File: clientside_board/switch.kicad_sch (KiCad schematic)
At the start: 23 parts, among them J5 Screw_Terminal_01x11, J6 Screw_Terminal_01x12, J7 Fire Button Connector, J8 Keylock Switch Connector, Q1 TSM2306CX

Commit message: Cleanup Power and Ethernet Sheet
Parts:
- renumbered J8 to J10, J5 to J7, J6 to J8, J7 to J9, R24 to R13, R8 to R14, R25 to R15, R9 to R16, R26 to R17, R10 to R18, R27 to R19, R11 to R20, R13 to R21, R16 to R22, R12 to R23, R17 to R24, R5 to R25, R14 to R26, R18 to R27, R6 to R28, R7 to R29, R15 to R30

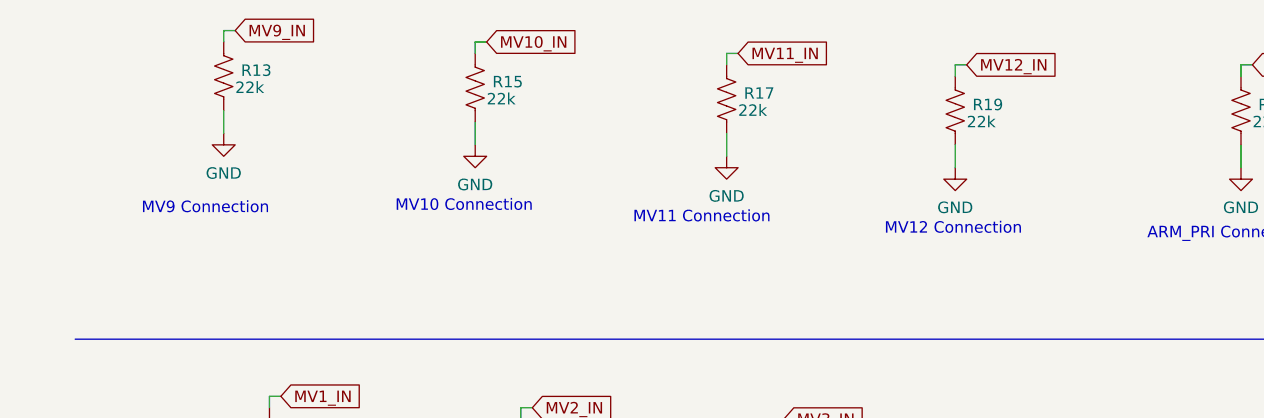
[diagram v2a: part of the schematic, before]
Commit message: Fix decoupling cap
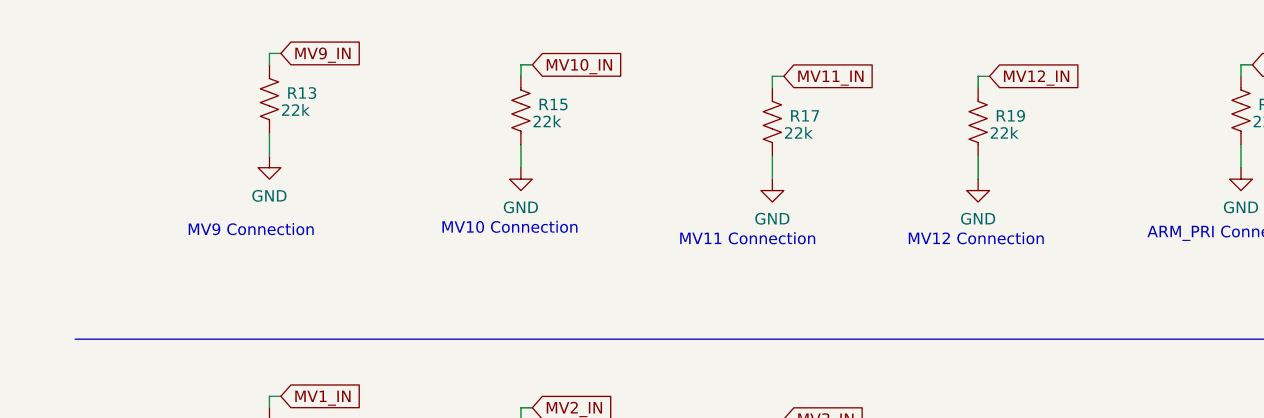
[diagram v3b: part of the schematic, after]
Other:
- moved on the sheet: R13, R15, R17, R19

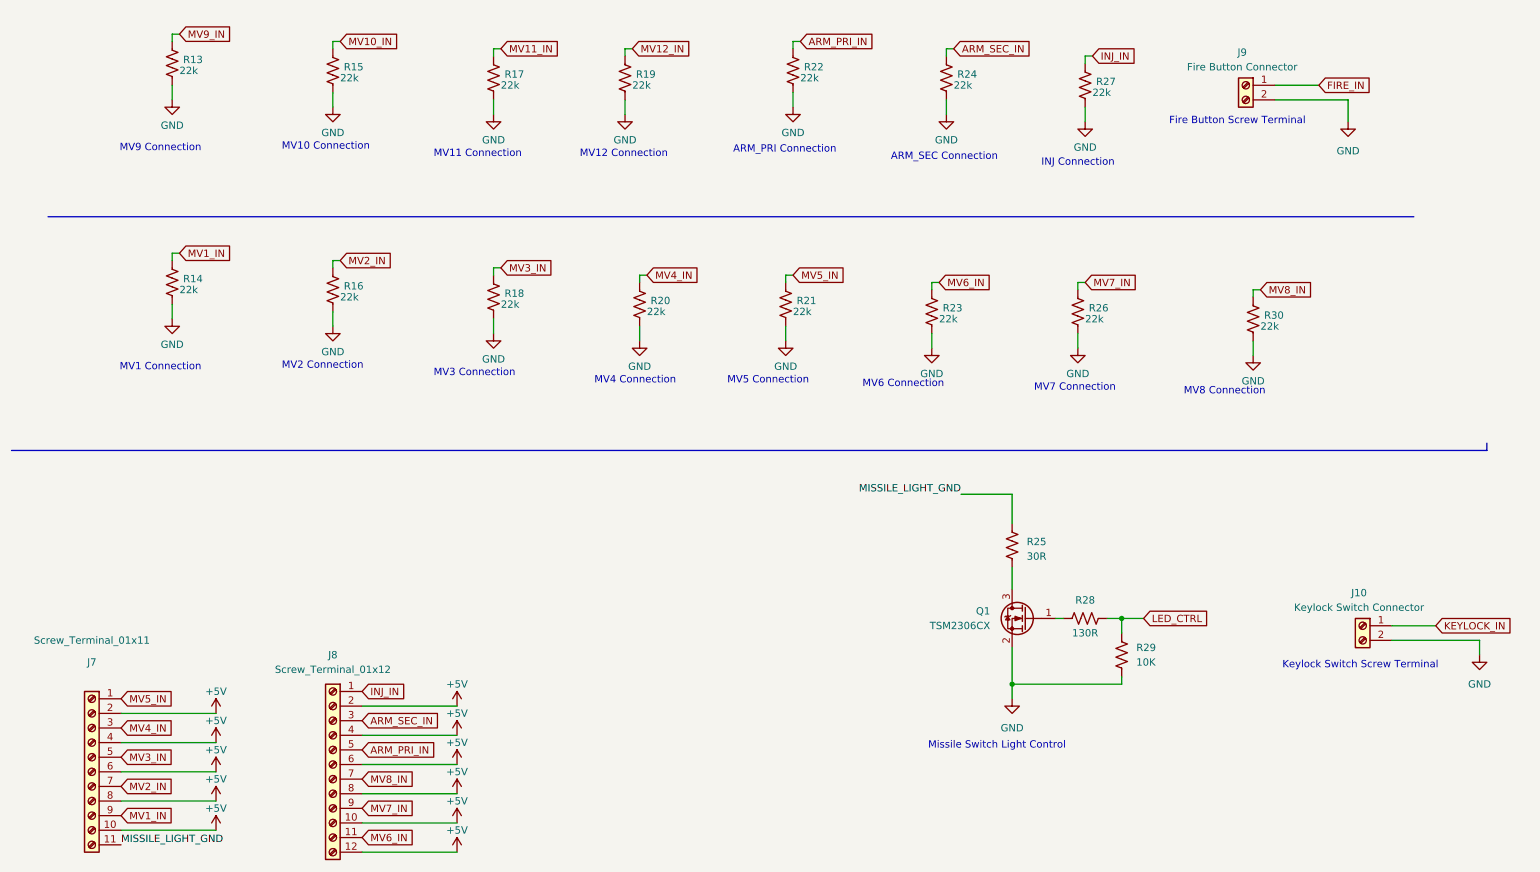
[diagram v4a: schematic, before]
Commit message: Clean-up missile switch connection sheet
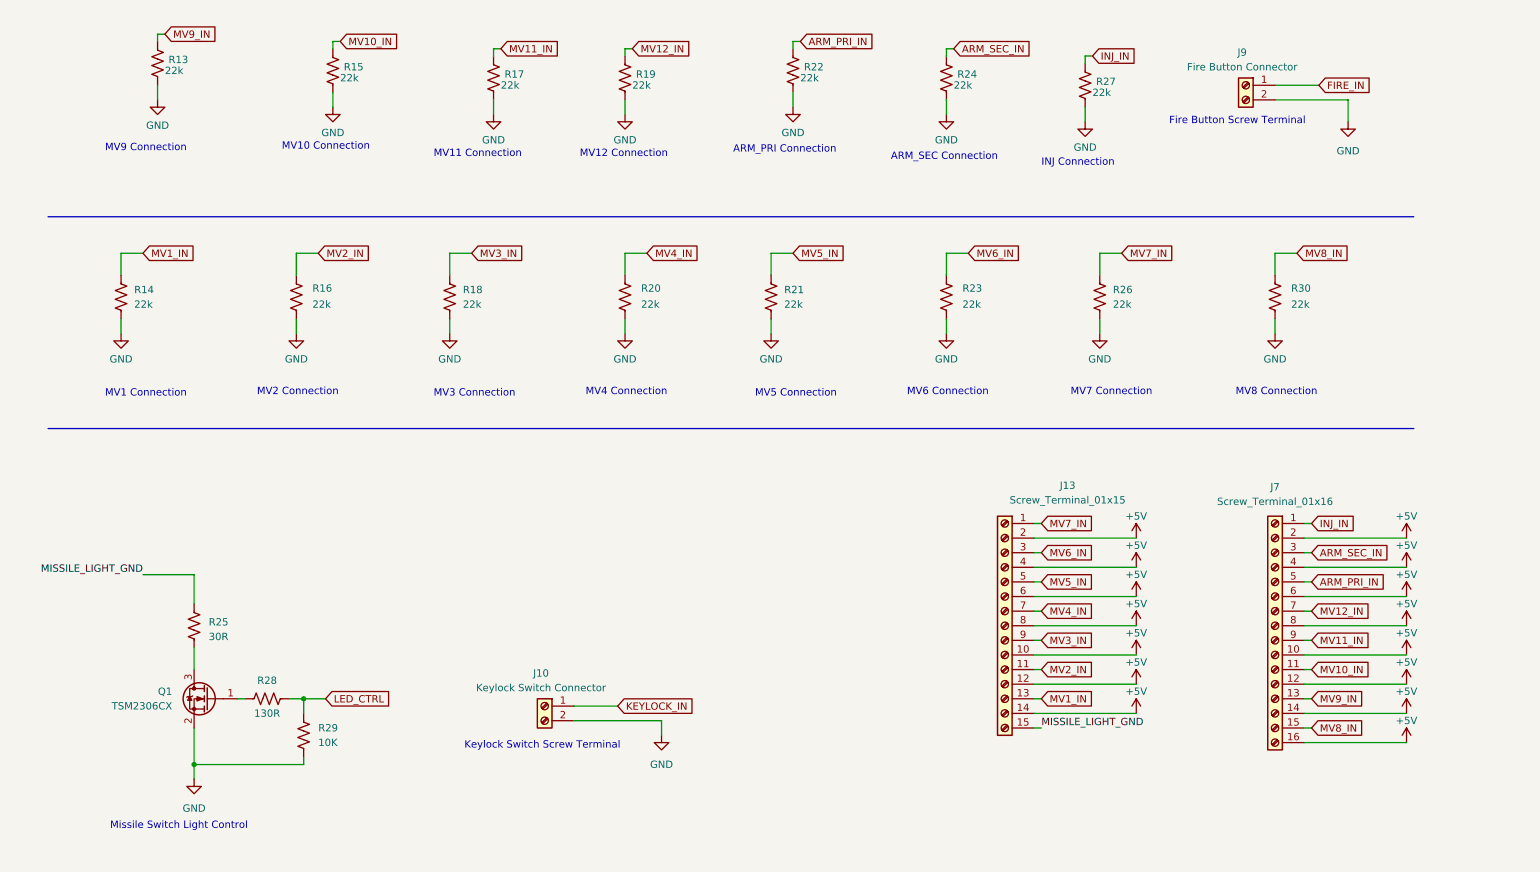
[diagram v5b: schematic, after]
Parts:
- removed J7: Screw_Terminal_01x11, TerminalBlock_Phoenix:TerminalBlock_Phoenix_PT-1,5-11-3.5-H_1x11_P3.50mm_Horizontal, symbol Connector:Screw_Terminal_01x11
- removed J8: Screw_Terminal_01x12, TerminalBlock_Phoenix:TerminalBlock_Phoenix_PT-1,5-12-3.5-H_1x12_P3.50mm_Horizontal, symbol Connector:Screw_Terminal_01x12
- added J13: Screw_Terminal_01x15, symbol Connector:Screw_Terminal_01x15
- added J7: Screw_Terminal_01x16, symbol Connector:Screw_Terminal_01x16
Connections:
- net +5V: now also J13.10 (Pin_10), J13.12 (Pin_12), J13.14 (Pin_14), J13.2 (Pin_2), J13.4 (Pin_4), J13.6 (Pin_6), J13.8 (Pin_8), J7.10 (Pin_10), J7.12 (Pin_12), J7.14 (Pin_14), J7.16 (Pin_16), J7.2 (Pin_2), J7.4 (Pin_4), J7.6 (Pin_6), J7.8 (Pin_8)
- net ARM_PRI_IN: now also J7.5 (Pin_5)
- net ARM_SEC_IN: now also J7.3 (Pin_3)
- net INJ_IN: now also J7.1 (Pin_1)
- net MISSILE_LIGHT_GND: now also J13.15 (Pin_15)
- net MV10_IN: now also J7.11 (Pin_11)
- net MV11_IN: now also J7.9 (Pin_9)
- net MV12_IN: now also J7.7 (Pin_7)
- net MV1_IN: now also J13.13 (Pin_13)
- net MV2_IN: now also J13.11 (Pin_11)
- net MV3_IN: now also J13.9 (Pin_9)
- net MV4_IN: now also J13.7 (Pin_7)
- net MV5_IN: now also J13.5 (Pin_5)
- net MV6_IN: now also J13.3 (Pin_3)
- net MV7_IN: now also J13.1 (Pin_1)
- net MV8_IN: now also J7.15 (Pin_15)
- net MV9_IN: now also J7.13 (Pin_13)
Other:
- title: (none) -> Missile Switch and Fire Button connections
- moved on the sheet: J10, Q1, R13, R14, R16, R25, R28, R29

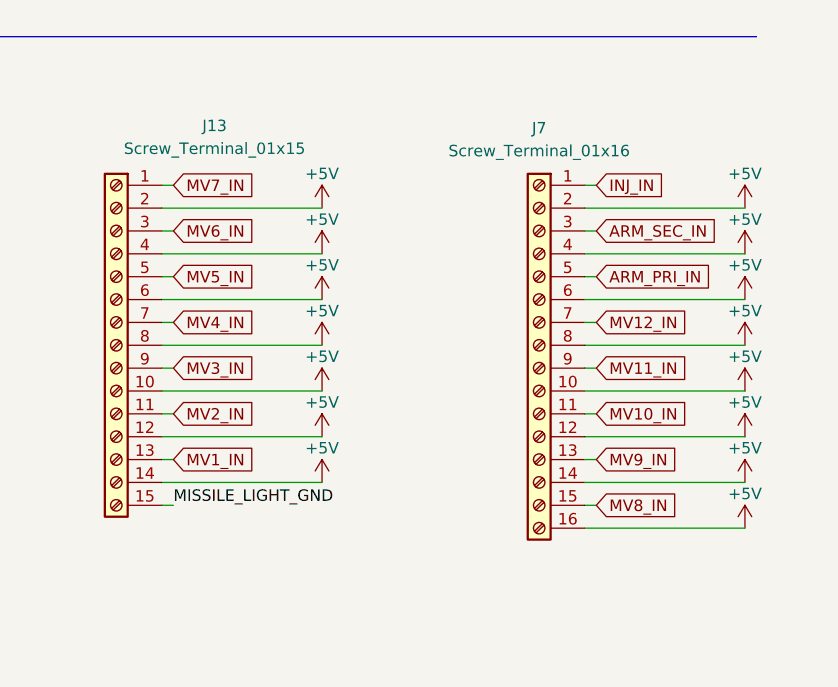
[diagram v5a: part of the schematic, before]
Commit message: Update power for 5V LCD display
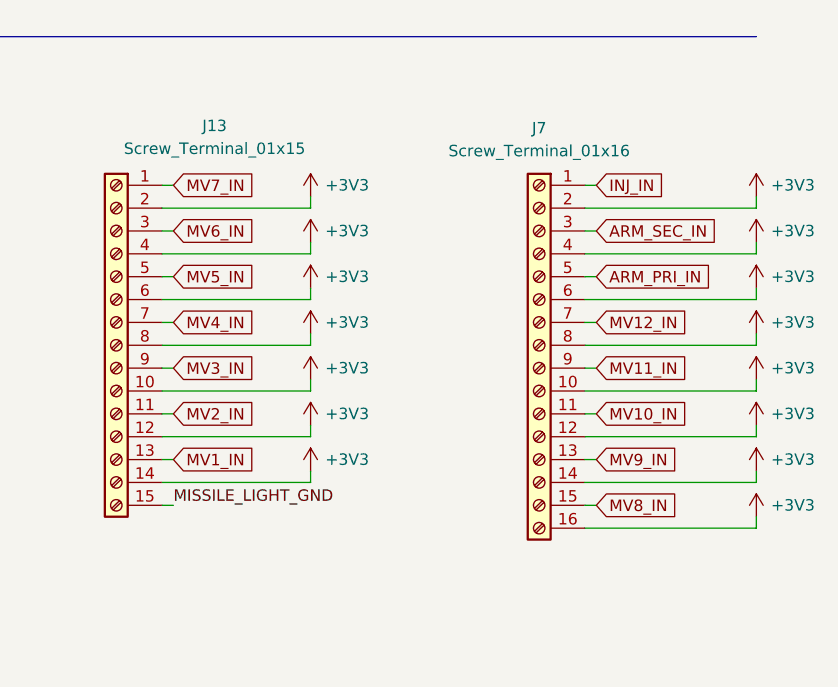
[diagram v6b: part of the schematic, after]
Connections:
- net +5V renamed +3V3

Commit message: Top sheet update
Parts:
- renumbered J7 to J10, J10 to J7, J13 to J8, R13 to R15, R25 to R16, R28 to R17, R16 to R18, R29 to R19, R15 to R20, R18 to R21, R17 to R22, R19 to R23, R20 to R24, R21 to R25, R22 to R26, R24 to R27, R23 to R28, R27 to R29, R26 to R30, R30 to R31
